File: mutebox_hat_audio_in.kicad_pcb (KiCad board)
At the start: 2 copper layers, 65 x 56 mm, 52 parts, among them J1 GPIO, J2 PLR237/T10BK, J3 RCJ-042, J4 RCJ-042, U1 CAT24C256, U2 74LVC157, U3 PCM1862DBT, U4 DIR9001PW, Y1 12.288 MHz, Y3 XO32

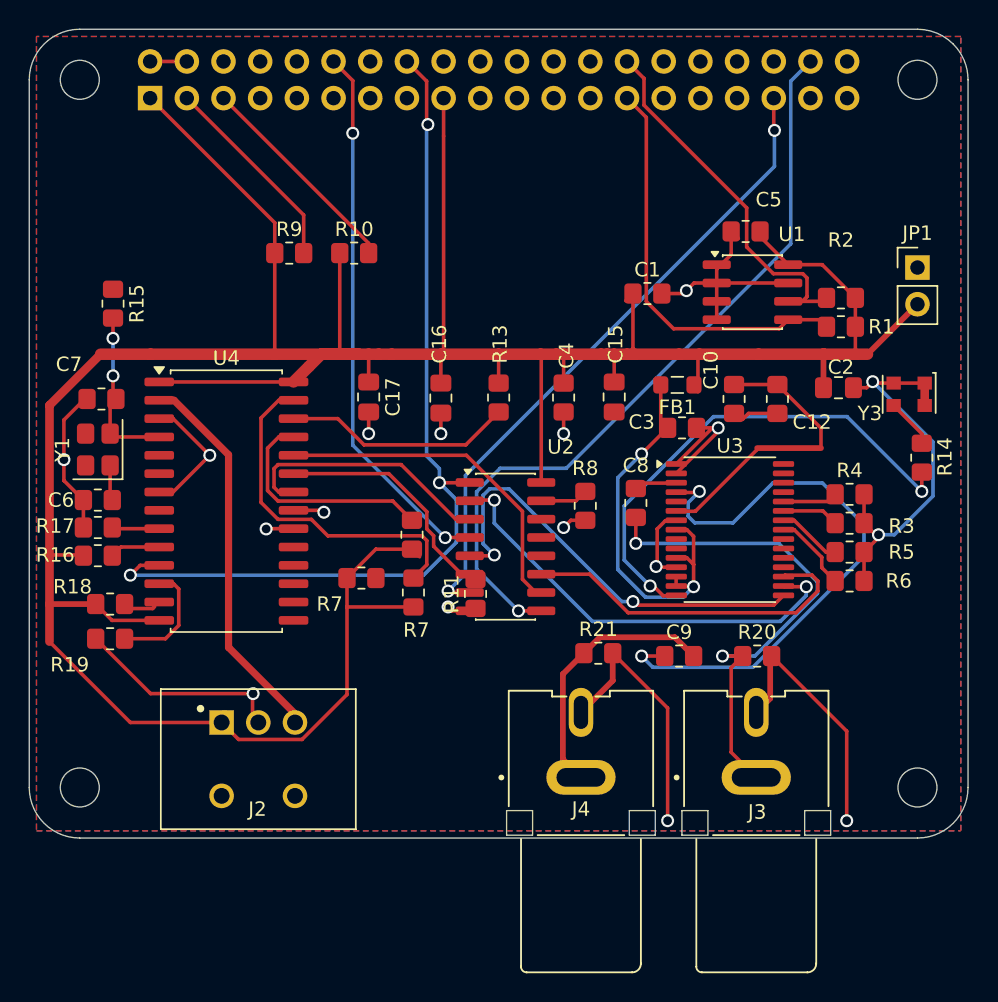
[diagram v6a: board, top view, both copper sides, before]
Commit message: fixed cooper fill zone issue.  Fixed broken routes
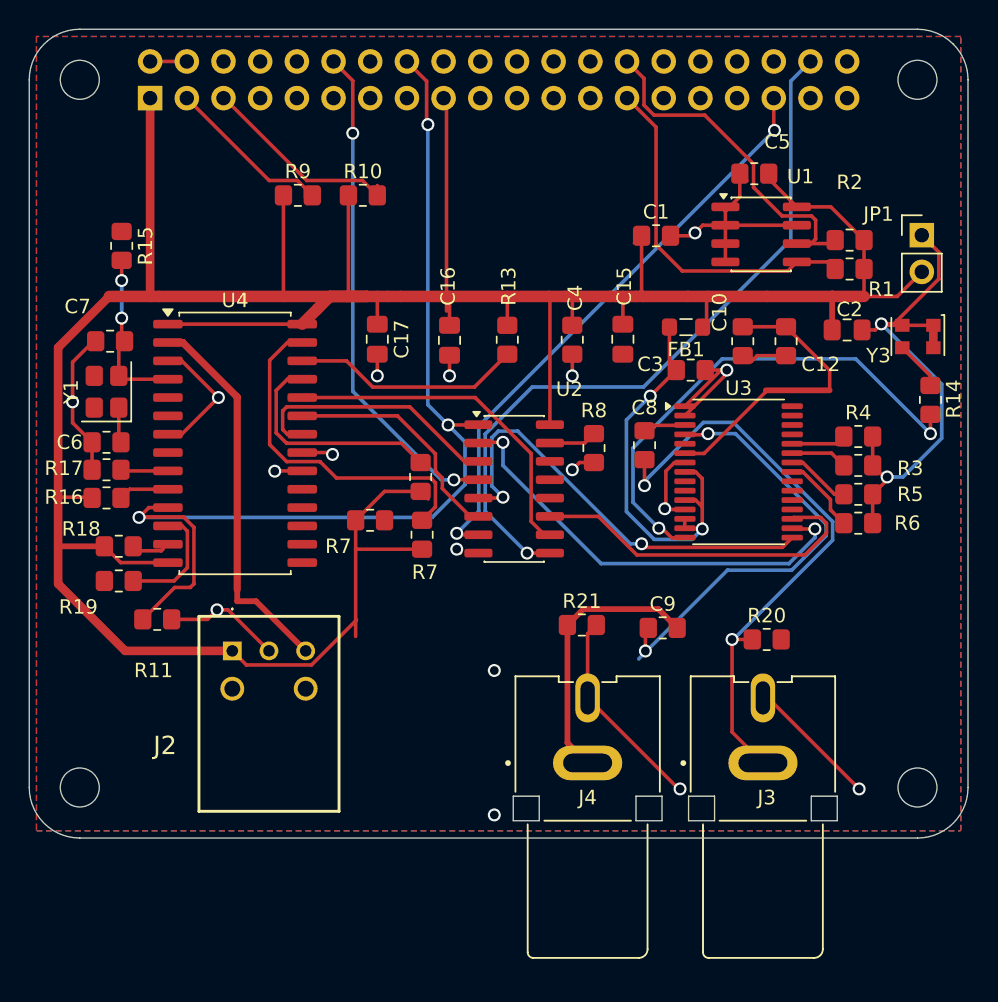
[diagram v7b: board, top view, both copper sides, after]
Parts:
- J2: footprint Connector_Audio:PLR237-T10BK -> RCJ-042:PLR237T10BK
- moved R11 22.1 mm to (108.9, 84.9), turned to 180 degrees
- moved J2 7.71 mm to (114.1, 87.0), turned to 0 degrees
- moved C3 4.04 mm to (145.8, 67.6)
- moved R2 4.04 mm to (156.8, 58.6)
- moved U1 4.04 mm to (150.7, 58.2)
- moved U3 4.04 mm to (149.1, 74.7)
- moved R15 4.04 mm to (106.4, 59.0)
- moved R18 4.04 mm to (106.2, 79.8)
- moved R19 4.04 mm to (106.2, 82.2)
- moved R7 4.04 mm to (127.2, 79.0)
- moved C1 4.04 mm to (143.4, 58.3)
- moved C10 4.04 mm to (149.4, 65.6)
- moved C12 4.04 mm to (152.4, 65.6)
- moved C15 4.04 mm to (141.1, 65.5)
- moved C16 4.04 mm to (129.1, 65.5)
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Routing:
- net GND: track 147.2 -> 136.4 mm, vias 17 -> 19
- net Net-(U3-VINR1/VIN2P): track 41.1 -> 31.8 mm
- net GPIO23_OPT_LOCK: track 62.9 -> 71.8 mm
- net Net-(C8-Pad2): track 35.6 -> 41.6 mm
- net +3V3: track 236.8 -> 231.0 mm
- net I2S_LRCLK: track 45.1 -> 40.8 mm
- net /ID_SDA: track 28.3 -> 24.6 mm
- net I2S_BCLK: track 37.9 -> 34.6 mm
- net I2S_DOUT: track 53.4 -> 50.9 mm
- net /GPIO2/SDA1: track 14.1 -> 12.1 mm
- net ID_SCL: track 26.8 -> 25.1 mm
- net /GPIO3/SCL1: track 14.9 -> 14.1 mm

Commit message: PCB tweaks
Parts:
- moved R20 1.18 mm to (151.6, 85.2)
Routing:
- net Net-(C8-Pad2): track 41.6 -> 42.6 mm
- net +3V3: track 231.0 -> 231.9 mm
- net Net-(U3-VINR1/VIN2P): track 31.8 -> 31.1 mm
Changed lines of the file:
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@@
 	(footprint "Resistor_SMD:R_0805_2012Metric_Pad1.20x1.40mm_HandSolder"
 		(layer "F.Cu")
-		(at 151.062 86.25)
+		(at 151.6 85.2)
 		(descr "Resistor SMD 0805 (2012 Metric), square (rectangular) end terminal, IPC-7351 nominal with elongated pad for handsoldering. (Body size source: IPC-SM-782 page 72, https://www.pcb-3d.com/wordpress/wp-content/uploads/ipc-sm-782a_amendment_1_and_2.pdf), generated with kicad-footprint-generator")
 		(tags "resistor handsolder")
@@
 		)
 		(property "Value" "1uF (film preferred)"
-			(at 3.6 1.4 90)
+			(at 0.2 2 90)
 			(layer "F.Fab")
 			(effects
@@
 	)
 	(segment
-		(start 122.6 80)
-		(end 122.6 86.040273)
-		(width 0.25)
-		(layer "F.Cu")
-		(net 29)
-	)
-	(segment
 		(start 122.6 78)
 		(end 124.6 76)
@@
 	)
 	(segment
+		(start 122.6 84.840273)
+		(end 122.6 78)
+		(width 0.25)
+		(layer "F.Cu")
+		(net 29)
+	)
+	(segment
 		(start 105.2 79.8)
 		(end 102 79.8)
@@
 	)
 	(segment
+		(start 122.66 84.900273)
+		(end 122.6 84.840273)
+		(width 0.25)
+		(layer "F.Cu")
+		(net 29)
+	)
+	(segment
 		(start 115.036 88.016)
 		(end 114.06 87.04)
@@
 	)
 	(segment
-		(start 155.176 79.06181)
-		(end 155.176 78.27857)
+		(start 148.261 81.451)
+		(end 152.78681 81.451)
 		(width 0.25)
 		(layer "B.Cu")
@@
 	)
 	(segment
-		(start 148.89743 72)
-		(end 147 72)
+		(start 155.176 79.06181)
+		(end 155.176 78.27857)
 		(width 0.25)
 		(layer "B.Cu")
@@
 	)
 	(segment
-		(start 142.2 87.6)
-		(end 148.349 81.451)
+		(start 148.89743 72)
+		(end 147 72)
 		(width 0.25)
 		(layer "B.Cu")
@@
 	)
 	(segment
-		(start 148.349 81.451)
-		(end 152.78681 81.451)
+		(start 142.662 87.05)
+		(end 148.261 81.451)
 		(width 0.25)
 		(layer "B.Cu")
@@
 	)
 	(segment
-		(start 154.4 78.6)
-		(end 152.875 78.6)
+		(start 154.400707 78.599293)
+		(end 154.307323 78.599293)
 		(width 0.25)
 		(layer "F.Cu")
@@
 	)
 	(segment
+		(start 154.307323 78.599293)
+		(end 154.306616 78.6)
+		(width 0.25)
+		(layer "F.Cu")
+		(net 64)
+	)
+	(segment
 		(start 152.875 78.6)
 		(end 152.825 78.55)
@@
 	)
 	(segment
+		(start 154.306616 78.6)
+		(end 152.875 78.6)
+		(width 0.25)
+		(layer "F.Cu")
+		(net 64)
+	)
+	(segment
 		(start 132.8 72.6)
 		(end 131.532322 72.6)
@@
 	)
 	(via
-		(at 154.4 78.6)
+		(at 154.400707 78.599293)
 		(size 0.9)
 		(drill 0.6)
@@
 	)
 	(segment
-		(start 139.6 81)
-		(end 132.8 74.2)
+		(start 154.400707 78.642677)
+		(end 154.4 78.643384)
 		(width 0.25)
 		(layer "B.Cu")
@@
 	)
 	(segment
-		(start 154.4 79.2)
-		(end 152.6 81)
+		(start 139.6 81)
+		(end 132.8 74.2)
 		(width 0.25)
 		(layer "B.Cu")
@@
 	)
 	(segment
+		(start 154.4 78.643384)
+		(end 154.4 79.2)
+		(width 0.25)
+		(layer "B.Cu")
+		(net 64)
+	)
+	(segment
 		(start 152.6 81)
 		(end 139.6 81)
@@
 	)
 	(segment
-		(start 154.4 78.6)
-		(end 154.4 79.2)
+		(start 154.400707 78.599293)
+		(end 154.400707 78.642677)
+		(width 0.25)
+		(layer "B.Cu")
+		(net 64)
+	)
+	(segment
+		(start 154.4 79.2)
+		(end 152.6 81)
 		(width 0.25)
 		(layer "B.Cu")
@@
 	)
 	(segment
-		(start 150.062 86.25)
+		(start 150.6 85.2)
+		(end 149.55 86.25)
+		(width 0.25)
+		(layer "F.Cu")
+		(net 81)
+	)
+	(segment
+		(start 149.55 86.25)
 		(end 148.662 86.25)
 		(width 0.25)
